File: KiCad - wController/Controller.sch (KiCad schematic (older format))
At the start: 9 parts, among them IC4 ATMEGA8-P, SW1 Reverse, SW2 Start, SW3 Lights, U5 Linkura

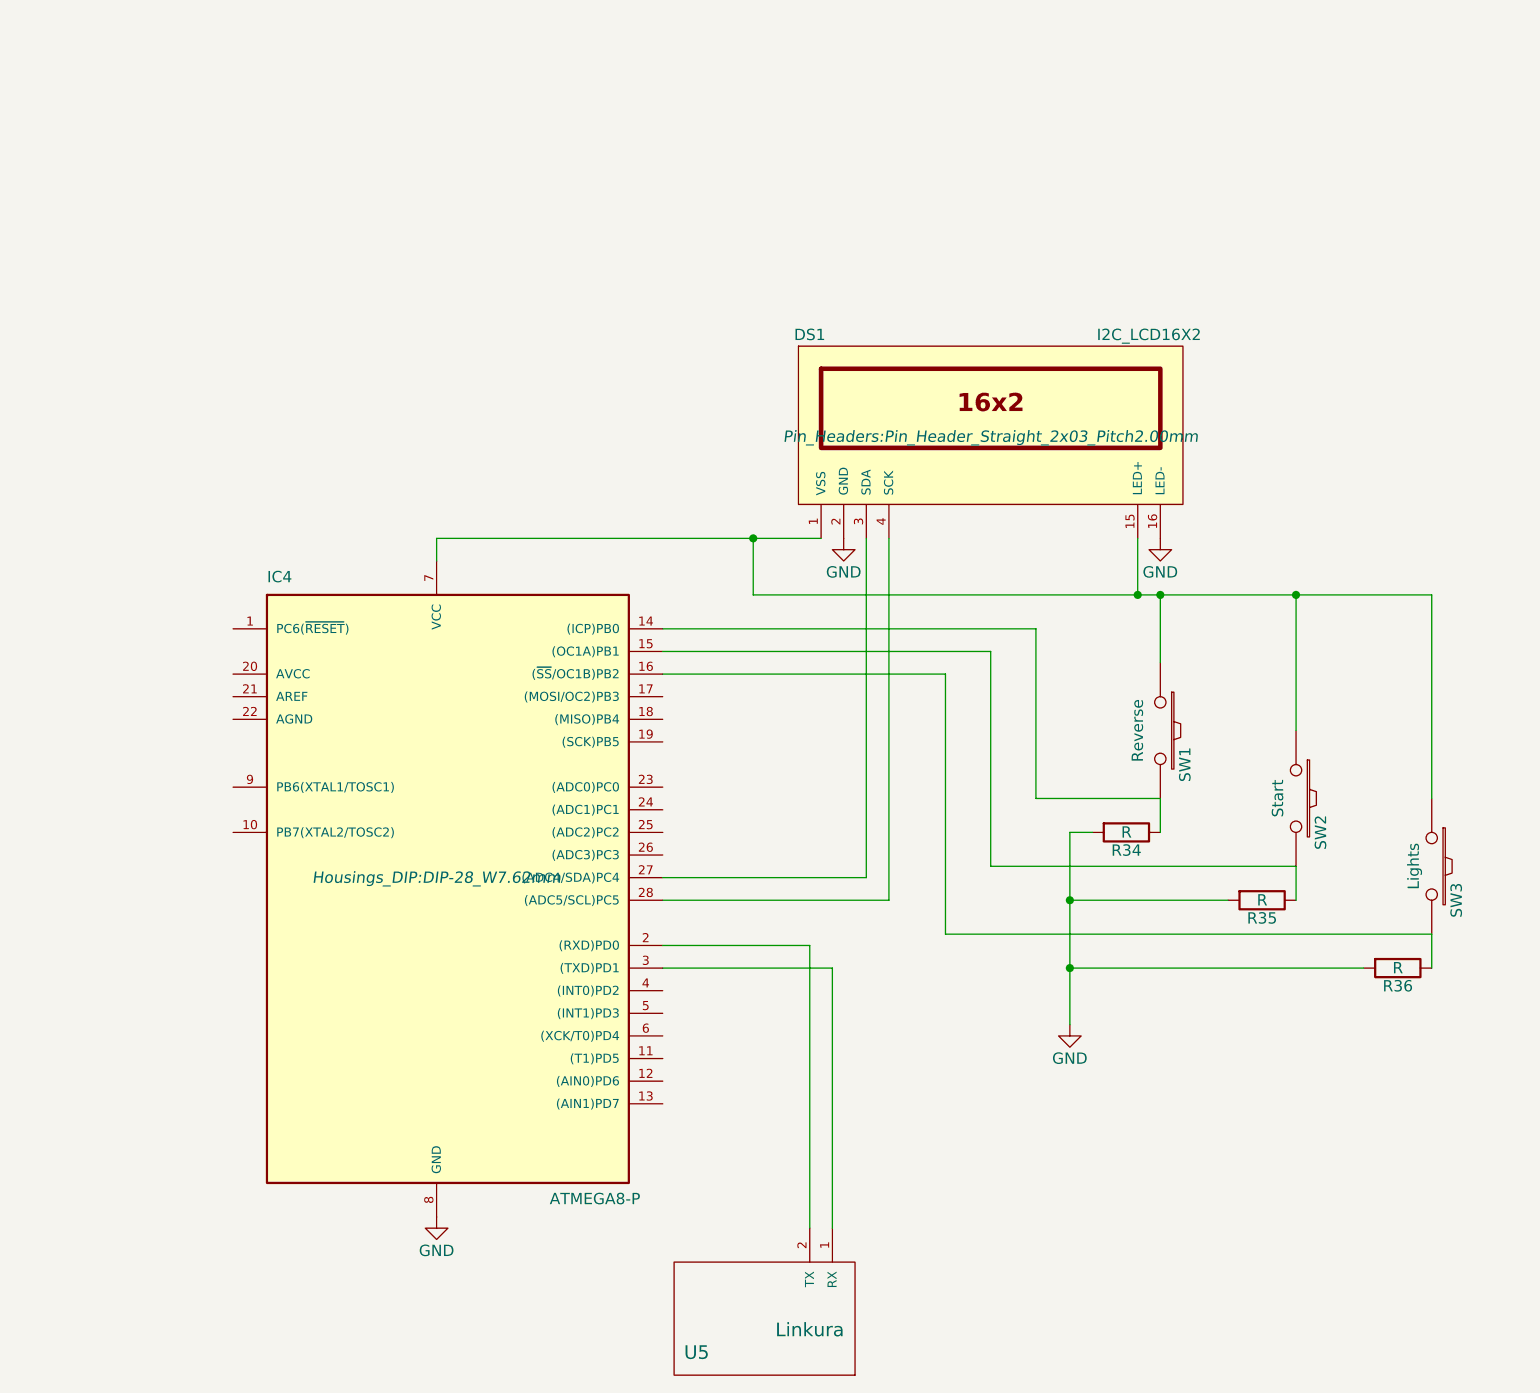
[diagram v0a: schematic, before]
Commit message: Added code and created PCB for controller
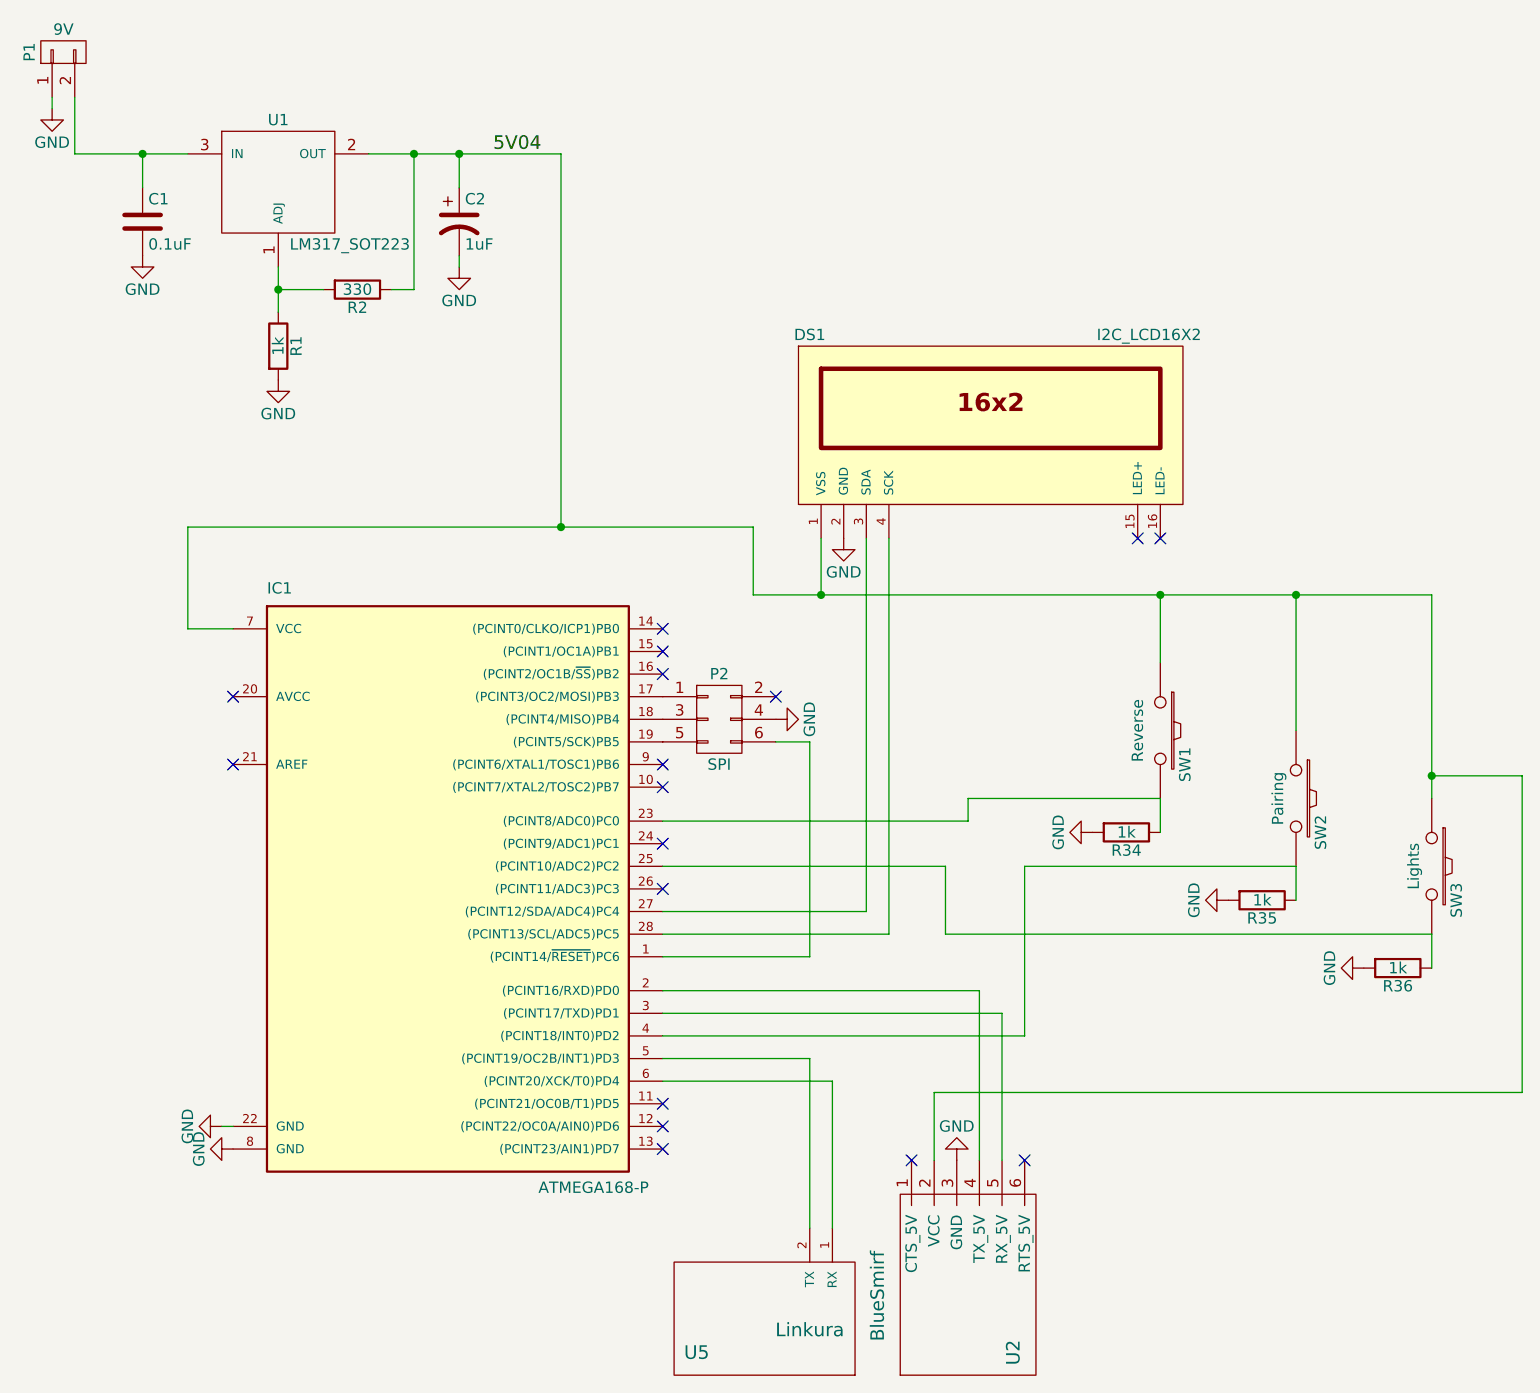
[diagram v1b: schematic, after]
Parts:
- removed IC4: ATMEGA8-P, Housings_DIP:DIP-28_W7.62mm, symbol ATMEGA8-P
- added C1: 0.1uF, Capacitors_ThroughHole:C_Disc_D6_P5, symbol C
- added C2: 1uF, Capacitors_ThroughHole:C_Radial_D5_L11_P2, symbol CP1
- added IC1: ATMEGA168-P, Housings_DIP:DIP-28_W7.62mm, symbol ATMEGA168-P
- added P1: 9V, Holes:SolderWirePad1mmmodified, symbol CONN_01X02
- added P2: SPI, Pin_Headers:Pin_Header_Straight_2x03, symbol CONN_02X03
- added R1: 1k, Resistors_ThroughHole:Resistor_Vertical_RM5mm, symbol R
- added R2: 330, Resistors_ThroughHole:Resistor_Vertical_RM5mm, symbol R
- added U1: LM317_SOT223, TO_SOT_Packages_THT:TO-220_Neutral123_Vertical, symbol LM317_SOT223
- added U2: BlueSmirf, Pin_Headers:Pin_Header_Straight_1x06, symbol BlueSmirf
- DS1: footprint Pin_Headers:Pin_Header_Straight_2x03_Pitch2.00mm -> Pin_Headers:Pin_Header_Straight_1x04
- R34, R35, R36: value R -> 1k
- SW1, SW3: footprint Wire_Connections_Bridges:WireConnection_1.50mmDrill -> Holes:SolderWirePad1mmmodified
- SW2: value Start -> Pairing; footprint Wire_Connections_Bridges:WireConnection_1.50mmDrill -> Holes:SolderWirePad1mmmodified
- U5: footprint Wire_Connections_Bridges:WireConnection_1.50mmDrill -> Pin_Headers:Pin_Header_Straight_1x02
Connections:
- net GND: now also C1.2, C2.2, IC1.22 (GND), IC1.8 (GND), P1.1 (P1), P2.4 (P4), R1.2, U2.3 (GND); no longer DS1.16 (LED-)
- net at U5.1 (RX): now also IC1.6 ((PCINT20/XCK/T0)PD4)
- net at U5.2 (TX): now also IC1.5 ((PCINT19/OC2B/INT1)PD3)
- net at R34.1, SW1.2: now also IC1.23 ((PCINT8/ADC0)PC0)
- net at R35.1, SW2.2: now also IC1.4 ((PCINT18/INT0)PD2)
- net at R36.1, SW3.2: now also IC1.25 ((PCINT10/ADC2)PC2)
- net at DS1.3 (SDA): now also IC1.27 ((PCINT12/SDA/ADC4)PC4)
- net at DS1.4 (SCK): now also IC1.28 ((PCINT13/SCL/ADC5)PC5)
- net 5V04: now reaches DS1.1 (VSS), SW1.1, SW2.1, SW3.1
- net 5V04: now also C2.1, IC1.7 (VCC), R2.1, U1.2 (OUT), U2.2 (VCC); no longer DS1.15 (LED+)
- new net: IC1.2 ((PCINT16/RXD)PD0), U2.4 (TX_5V)
- new net: IC1.3 ((PCINT17/TXD)PD1), U2.5 (RX_5V)
- new net: R1.1, R2.2, U1.1 (ADJ)
- new net: C1.1, P1.2 (P2), U1.3 (IN)
- new net: IC1.17 ((PCINT3/OC2/MOSI)PB3), P2.1 (P1)
- new net: IC1.18 ((PCINT4/MISO)PB4), P2.3 (P3)
- new net: IC1.19 ((PCINT5/SCK)PB5), P2.5 (P5)
- new net: IC1.1 ((PCINT14/~RESET~)PC6), P2.6 (P6)
- no-connect marks 0 -> 17

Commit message: Working ADC!
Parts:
- U5: symbol Linkura -> Linkura-RESCUE-Project
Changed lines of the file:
@@
 EESchema Schematic File Version 2
+LIBS:Project-rescue
 LIBS:power
 LIBS:device
@@
 $EndDescr
 $Comp
-L Linkura U5
+L Linkura-RESCUE-Project U5
 U 1 1 5717C731
 P 4000 6600
